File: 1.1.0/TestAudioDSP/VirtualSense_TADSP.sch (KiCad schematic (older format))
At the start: 37 parts, among them P2 CONN_1, P3 CONN_1, P5 CONN_1, P6 CONN_1, P7 uC, P8 uC, U1 MSP430F5435A, U2 24AA1025, U3 PCF2123, U4 24AA025E48, X1 32.6768kHz

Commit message: edited schematics of audio DSP test layer adding libraries of CC5535, DC regulator, AIC3204, 12MHz OSC
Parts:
- removed C1, C10, C11, C2, C3, C4, C7: 100n, symbol CSMALL
- removed C5: 10u, symbol CSMALL
- removed C6: 0,47uF, symbol CSMALL
- removed C8, C9: 18p, symbol CSMALL
- removed FB1, FB2: 10n, symbol FILTER
- removed JP1, JP2, JP3: BREAKER, symbol BREAKER
- removed R1, R2, R9: 47K, symbol R
- removed R7, R8: 10K, symbol R
- removed U1: MSP430F5435A, symbol MSP430F5435A
- removed U2: 24AA1025, symbol 24AA512
- removed U3: PCF2123, symbol PCF2123
- removed U4: 24AA025E48, symbol 24AA512
- removed X1: 32.6768kHz, symbol QUARZO_2PIN
- added U?: TPS77801, symbol TPS77801
- added U?: TPS79501DCQ, symbol TPS79501DCQ
- added U?: DSX321G_12MHZ, symbol DSX321G_12MHZ
- gave numbers to parts that had none: 1
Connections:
- net labels removed: AGND, AVcc, DGND, DVcc, E0_EN/P4.5, E1_EN/P4.4, GNDPWR, RTC_EN/P3.6, RTC_INT/P2.4
- wire segments 245 -> 58
- no-connect marks 17 -> 4
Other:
- moved on the sheet: U2

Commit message: schematics of audio DSP test layer OK, added module on audio DSP test layer brd
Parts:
- removed CONN2, CONN4: CONN_14, symbol CONN_14
- added C1, C16, C17, C23: 4u7, symbol CP1SMALL
- added C10: 33p, symbol CSMALL
- added C11, C12, C20, C21, C7: 10u, symbol CP1SMALL
- added C13, C2: 1u, symbol CSMALL
- added C14, C15, C18, C19, C22, C3, C9: 100n, symbol CSMALL
- added C4, C5: 470n, symbol CSMALL
- added C6, C8: NO, symbol CSMALL
- added JP1: JUMPER, symbol JUMPER
- added L1, L2: BLM21AG151SN1D, symbol FILTER
- added M1: MIC, symbol SPEAKER
- added P1: 1V8CC, symbol CONN_1
- added P4: 1V3CC, symbol CONN_1
- added P9: MC-D, symbol CONN_1
- added Q1: MOS_N, symbol MOS_N
- added R1: 2K2, symbol RSML
- added R10: 110K, symbol RSML
- added R11, R8: 0-NO, symbol RSML
- added R12, R7: 0, symbol RSML
- added R13, R3: 4K7, symbol RSML
- added R14, R15: 300, symbol RSML
- added R2: 1K, symbol RSML
- added R4: 250K, symbol RSML
- added R5: 14K, symbol RSML
- added R6: 30K, symbol RSML
- added R9: 10K7, symbol RSML
- gave numbers to parts that had none: 3
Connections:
- net labels added: CPU_CLK_12MHZ, GND-AIC, GNDPWR, I2C_SCL, I2C_SDA, I2S2_CLK, I2S2_DX, I2S2_FS, I2S2_RX, MCLK, MICN, MICP, TARGET_PWR_GOOD, V3.3A, VCC_1V3, VCC_1V8
- net labels removed: ADC0/P6.0, ADC1/P6.1, ADC2/P6.2, ADC3/P6.3, ADC4/P6.4, ADC5/P6.5, ADC6/P6.6, CLKOUT, DIO2/P8.5, DIO3/P8.6, INT0/P2.0, INT1/P2.3, INT2/P2.5, INT3/P2.6, INT4/P2.7, LED0/P8.0, LED1/P8.1, LED2/P8.2, RXD2/MISO3/P5.7, SCL/P3.2, SDA/P3.1, SN0_EN/P8.3, SN1_EN/P8.4, TXD2/MOSI3/P5.6, VREF+/P5.0, VREF-/P5.1
- wire segments 58 -> 182
- no-connect marks 4 -> 14
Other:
- moved on the sheet: U1, U2, U3, U4

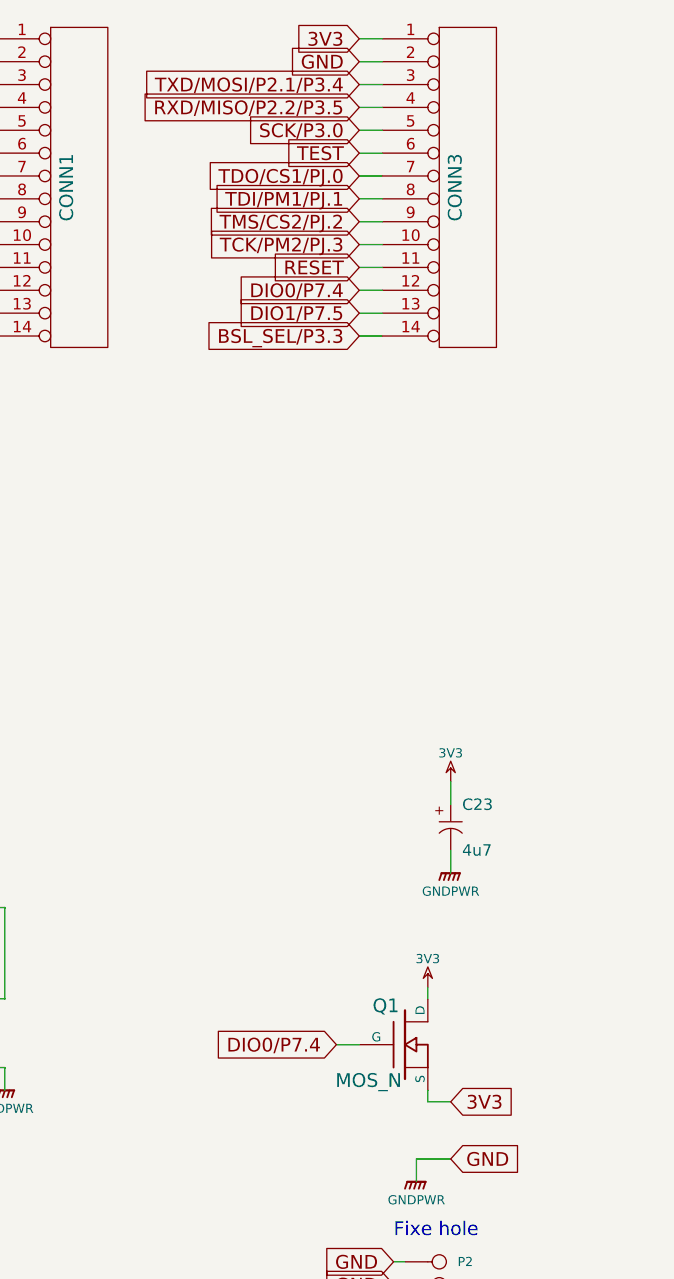
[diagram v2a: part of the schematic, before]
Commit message: audio DSP test layer: brd OK, gerber Ok - sent to PCBoards for check
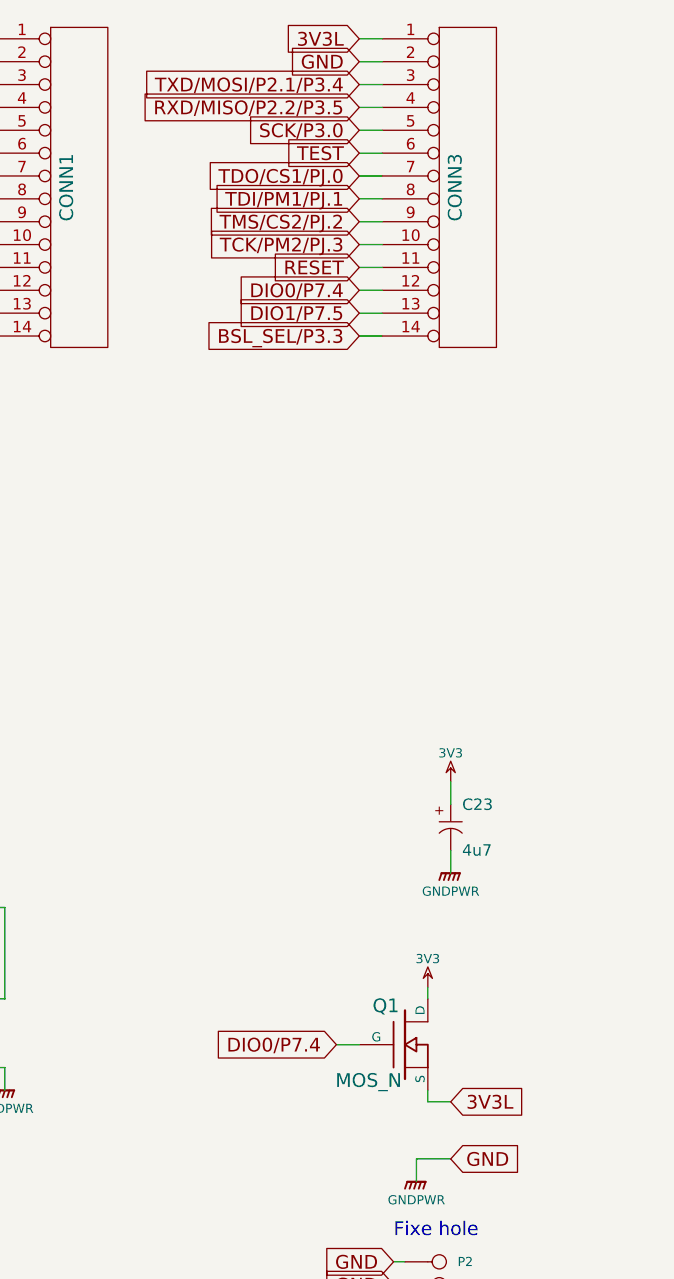
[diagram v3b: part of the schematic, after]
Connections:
- net labels added: 3V3L
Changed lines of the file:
@@
 $EndDescr
 Text GLabel 10400 750  0    60   Input ~ 0
-3V3
+3V3L
 Text GLabel 10400 850  0    60   Input ~ 0
 GND
@@
 $EndSheet
 Text GLabel 10800 5400 2    60   Input ~ 0
-3V3
-$Comp
-L GNDPWR #PWR01
+3V3L
+$Comp
+L GNDPWR #PWR22
 U 1 1 521DAD52
 P 10650 5750
-F 0 "#PWR01" H 10650 5800 40  0001 C CNN
+F 0 "#PWR22" H 10650 5800 40  0001 C CNN
 F 1 "GNDPWR" H 10650 5670 40  0000 C CNN
 F 2 "" H 10650 5750 60  0001 C CNN
@@
 GND
 $Comp
-L GNDPWR #PWR02
+L GNDPWR #PWR4
 U 1 1 521DADD2
 P 1250 1500
-F 0 "#PWR02" H 1250 1550 40  0001 C CNN
+F 0 "#PWR4" H 1250 1550 40  0001 C CNN
 F 1 "GNDPWR" H 1250 1420 40  0000 C CNN
 F 2 "" H 1250 1500 60  0001 C CNN
@@
 $EndComp
 $Comp
-L 3V3 #PWR03
+L 3V3 #PWR1
 U 1 1 521DAE7E
 P 1000 1050
-F 0 "#PWR03" H 1000 1150 40  0001 C CNN
+F 0 "#PWR1" H 1000 1150 40  0001 C CNN
 F 1 "3V3" H 1000 1175 40  0000 C CNN
 F 2 "" H 1000 1050 60  0001 C CNN
@@
 $EndComp
 $Comp
-L GNDPWR #PWR04
+L GNDPWR #PWR10
 U 1 1 521DB683
 P 3350 1900
-F 0 "#PWR04" H 3350 1950 40  0001 C CNN
+F 0 "#PWR10" H 3350 1950 40  0001 C CNN
 F 1 "GNDPWR" H 3350 1820 40  0000 C CNN
 F 2 "" H 3350 1900 60  0001 C CNN
@@
 $EndComp
 $Comp
-L GNDPWR #PWR05
+L GNDPWR #PWR14
 U 1 1 521DB7CE
 P 3650 1600
-F 0 "#PWR05" H 3650 1650 40  0001 C CNN
+F 0 "#PWR14" H 3650 1650 40  0001 C CNN
 F 1 "GNDPWR" H 3650 1520 40  0000 C CNN
 F 2 "" H 3650 1600 60  0001 C CNN
@@
 VCC_1V3
 $Comp
-L 3V3 #PWR06
+L 3V3 #PWR8
 U 1 1 521DB933
 P 2950 1500
-F 0 "#PWR06" H 2950 1600 40  0001 C CNN
+F 0 "#PWR8" H 2950 1600 40  0001 C CNN
 F 1 "3V3" H 2950 1625 40  0000 C CNN
 F 2 "" H 2950 1500 60  0001 C CNN
@@
 TARGET_PWR_GOOD
 $Comp
-L 3V3 #PWR07
+L 3V3 #PWR2
 U 1 1 521DBAC4
 P 1000 2300
-F 0 "#PWR07" H 1000 2400 40  0001 C CNN
+F 0 "#PWR2" H 1000 2400 40  0001 C CNN
 F 1 "3V3" H 1000 2425 40  0000 C CNN
 F 2 "" H 1000 2300 60  0001 C CNN
@@
 $EndComp
 $Comp
-L GNDPWR #PWR08
+L GNDPWR #PWR3
 U 1 1 521DBAF7
 P 1000 2750
-F 0 "#PWR08" H 1000 2800 40  0001 C CNN
+F 0 "#PWR3" H 1000 2800 40  0001 C CNN
 F 1 "GNDPWR" H 1000 2670 40  0000 C CNN
 F 2 "" H 1000 2750 60  0001 C CNN
@@
 $EndComp
 $Comp
-L GNDPWR #PWR09
+L GNDPWR #PWR6
 U 1 1 521DBFAD
 P 2200 3050
-F 0 "#PWR09" H 2200 3100 40  0001 C CNN
+F 0 "#PWR6" H 2200 3100 40  0001 C CNN
 F 1 "GNDPWR" H 2200 2970 40  0000 C CNN
 F 2 "" H 2200 3050 60  0001 C CNN
@@
 $EndComp
 $Comp
-L GNDPWR #PWR010
+L GNDPWR #PWR12
 U 1 1 521DC2F6
 P 3550 2750
-F 0 "#PWR010" H 3550 2800 40  0001 C CNN
+F 0 "#PWR12" H 3550 2800 40  0001 C CNN
 F 1 "GNDPWR" H 3550 2670 40  0000 C CNN
 F 2 "" H 3550 2750 60  0001 C CNN
@@
 VCC_1V8
 $Comp
-L GNDPWR #PWR011
+L GNDPWR #PWR9
 U 1 1 521DC78D
 P 3000 3150
-F 0 "#PWR011" H 3000 3200 40  0001 C CNN
+F 0 "#PWR9" H 3000 3200 40  0001 C CNN
 F 1 "GNDPWR" H 3000 3070 40  0000 C CNN
 F 2 "" H 3000 3150 60  0001 C CNN
@@
 $EndComp
 $Comp
-L 3V3 #PWR012
+L 3V3 #PWR24
 U 1 1 521DCB4A
 P 10800 4000
-F 0 "#PWR012" H 10800 4100 40  0001 C CNN
+F 0 "#PWR24" H 10800 4100 40  0001 C CNN
 F 1 "3V3" H 10800 4125 40  0000 C CNN
 F 2 "" H 10800 4000 60  0001 C CNN
@@
 $EndComp
 $Comp
-L GNDPWR #PWR013
+L GNDPWR #PWR25
 U 1 1 521DCB50
 P 10800 4400
-F 0 "#PWR013" H 10800 4450 40  0001 C CNN
+F 0 "#PWR25" H 10800 4450 40  0001 C CNN
 F 1 "GNDPWR" H 10800 4320 40  0000 C CNN
 F 2 "" H 10800 4400 60  0001 C CNN
@@
 $EndComp
 $Comp
-L GNDPWR #PWR014
+L GNDPWR #PWR11
 U 1 1 521DCE8E
 P 3350 4450
-F 0 "#PWR014" H 3350 4500 40  0001 C CNN
+F 0 "#PWR11" H 3350 4500 40  0001 C CNN
 F 1 "GNDPWR" H 3350 4370 40  0000 C CNN
 F 2 "" H 3350 4450 60  0001 C CNN
@@
 $EndComp
 $Comp
-L 3V3 #PWR015
+L 3V3 #PWR7
 U 1 1 521DCFCF
 P 2800 4100
-F 0 "#PWR015" H 2800 4200 40  0001 C CNN
+F 0 "#PWR7" H 2800 4200 40  0001 C CNN
 F 1 "3V3" H 2800 4225 40  0000 C CNN
 F 2 "" H 2800 4100 60  0001 C CNN
@@
 $EndComp
 $Comp
-L GNDPWR #PWR016
+L GNDPWR #PWR19
 U 1 1 521DD2BC
 P 7150 6900
-F 0 "#PWR016" H 7150 6950 40  0001 C CNN
+F 0 "#PWR19" H 7150 6950 40  0001 C CNN
 F 1 "GNDPWR" H 7150 6820 40  0000 C CNN
 F 2 "" H 7150 6900 60  0001 C CNN
@@
 $EndComp
 $Comp
-L 3V3 #PWR017
+L 3V3 #PWR21
 U 1 1 521DD2C2
 P 8850 6800
-F 0 "#PWR017" H 8850 6900 40  0001 C CNN
+F 0 "#PWR21" H 8850 6900 40  0001 C CNN
 F 1 "3V3" H 8850 6925 40  0000 C CNN
 F 2 "" H 8850 6800 60  0001 C CNN
@@
 $EndComp
 $Comp
-L GNDPWR #PWR018
+L GNDPWR #PWR13
 U 1 1 521DDF50
 P 3600 3950
-F 0 "#PWR018" H 3600 4000 40  0001 C CNN
+F 0 "#PWR13" H 3600 4000 40  0001 C CNN
 F 1 "GNDPWR" H 3600 3870 40  0000 C CNN
 F 2 "" H 3600 3950 60  0001 C CNN
@@
 $EndComp
 $Comp
-L GNDPWR #PWR019
+L GNDPWR #PWR15
 U 1 1 521DE36F
 P 3850 7000
-F 0 "#PWR019" H 3850 7050 40  0001 C CNN
+F 0 "#PWR15" H 3850 7050 40  0001 C CNN
 F 1 "GNDPWR" H 3850 6920 40  0000 C CNN
 F 2 "" H 3850 7000 60  0001 C CNN
@@
 NoConn ~ 3250 6300
 $Comp
-L 3V3 #PWR020
+L 3V3 #PWR5
 U 1 1 521DECC8
 P 2100 6150
-F 0 "#PWR020" H 2100 6250 40  0001 C CNN
+F 0 "#PWR5" H 2100 6250 40  0001 C CNN
 F 1 "3V3" H 2100 6275 40  0000 C CNN
 F 2 "" H 2100 6150 60  0001 C CNN
@@
 $EndComp
 $Comp
-L GNDPWR #PWR021
+L GNDPWR #PWR16
 U 1 1 521DFB68
 P 5300 6550
-F 0 "#PWR021" H 5300 6600 40  0001 C CNN
+F 0 "#PWR16" H 5300 6600 40  0001 C CNN
 F 1 "GNDPWR" H 5300 6470 40  0000 C CNN
 F 2 "" H 5300 6550 60  0001 C CNN
@@
 I2S2_CLK
 $Comp
-L 3V3 #PWR022
+L 3V3 #PWR17
 U 1 1 521E0515
 P 6900 4500
-F 0 "#PWR022" H 6900 4600 40  0001 C CNN
+F 0 "#PWR17" H 6900 4600 40  0001 C CNN
 F 1 "3V3" H 6900 4625 40  0000 C CNN
 F 2 "" H 6900 4500 60  0001 C CNN
@@
 $EndComp
 $Comp
-L GNDPWR #PWR023
+L GNDPWR #PWR18
 U 1 1 521E0521
 P 6900 4900
-F 0 "#PWR023" H 6900 4950 40  0001 C CNN
+F 0 "#PWR18" H 6900 4950 40  0001 C CNN
 F 1 "GNDPWR" H 6900 4820 40  0000 C CNN
 F 2 "" H 6900 4900 60  0001 C CNN
@@
 $EndComp
 $Comp
-L GNDPWR #PWR024
+L GNDPWR #PWR20
 U 1 1 521E091E
 P 8850 5350
-F 0 "#PWR024" H 8850 5400 40  0001 C CNN
+F 0 "#PWR20" H 8850 5400 40  0001 C CNN
 F 1 "GNDPWR" H 8850 5270 40  0000 C CNN
 F 2 "" H 8850 5350 60  0001 C CNN
@@
 $EndComp
 $Comp
-L 3V3 #PWR025
+L 3V3 #PWR23
 U 1 1 521E0E79
 P 10700 4900
-F 0 "#PWR025" H 10700 5000 40  0001 C CNN
+F 0 "#PWR23" H 10700 5000 40  0001 C CNN
 F 1 "3V3" H 10700 5025 40  0000 C CNN
 F 2 "" H 10700 4900 60  0001 C CNN

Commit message: audio DSP test layer: renamed zip first gerber, added 0-Ohm (R35) for module U2, schematic OK, brd OK, gerber OK - 2nd sent to PCBoards for check
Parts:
- removed P9: MC-D, symbol CONN_1
- added R35: 0, symbol RSML
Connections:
- wire segments 182 -> 184
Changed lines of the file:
@@
 3V3L
 $Comp
-L GNDPWR #PWR22
+L GNDPWR #PWR01
 U 1 1 521DAD52
 P 10650 5750
-F 0 "#PWR22" H 10650 5800 40  0001 C CNN
+F 0 "#PWR01" H 10650 5800 40  0001 C CNN
 F 1 "GNDPWR" H 10650 5670 40  0000 C CNN
 F 2 "" H 10650 5750 60  0001 C CNN
@@
 GND
 $Comp
-L GNDPWR #PWR4
+L GNDPWR #PWR02
 U 1 1 521DADD2
 P 1250 1500
-F 0 "#PWR4" H 1250 1550 40  0001 C CNN
+F 0 "#PWR02" H 1250 1550 40  0001 C CNN
 F 1 "GNDPWR" H 1250 1420 40  0000 C CNN
 F 2 "" H 1250 1500 60  0001 C CNN
@@
 $EndComp
 $Comp
-L 3V3 #PWR1
+L 3V3 #PWR03
 U 1 1 521DAE7E
 P 1000 1050
-F 0 "#PWR1" H 1000 1150 40  0001 C CNN
+F 0 "#PWR03" H 1000 1150 40  0001 C CNN
 F 1 "3V3" H 1000 1175 40  0000 C CNN
 F 2 "" H 1000 1050 60  0001 C CNN
@@
 $EndComp
 $Comp
-L GNDPWR #PWR10
+L GNDPWR #PWR04
 U 1 1 521DB683
 P 3350 1900
-F 0 "#PWR10" H 3350 1950 40  0001 C CNN
+F 0 "#PWR04" H 3350 1950 40  0001 C CNN
 F 1 "GNDPWR" H 3350 1820 40  0000 C CNN
 F 2 "" H 3350 1900 60  0001 C CNN
@@
 $EndComp
 $Comp
-L GNDPWR #PWR14
+L GNDPWR #PWR05
 U 1 1 521DB7CE
 P 3650 1600
-F 0 "#PWR14" H 3650 1650 40  0001 C CNN
+F 0 "#PWR05" H 3650 1650 40  0001 C CNN
 F 1 "GNDPWR" H 3650 1520 40  0000 C CNN
 F 2 "" H 3650 1600 60  0001 C CNN
@@
 VCC_1V3
 $Comp
-L 3V3 #PWR8
+L 3V3 #PWR06
 U 1 1 521DB933
 P 2950 1500
-F 0 "#PWR8" H 2950 1600 40  0001 C CNN
+F 0 "#PWR06" H 2950 1600 40  0001 C CNN
 F 1 "3V3" H 2950 1625 40  0000 C CNN
 F 2 "" H 2950 1500 60  0001 C CNN
@@
 TARGET_PWR_GOOD
 $Comp
-L 3V3 #PWR2
+L 3V3 #PWR07
 U 1 1 521DBAC4
 P 1000 2300
-F 0 "#PWR2" H 1000 2400 40  0001 C CNN
+F 0 "#PWR07" H 1000 2400 40  0001 C CNN
 F 1 "3V3" H 1000 2425 40  0000 C CNN
 F 2 "" H 1000 2300 60  0001 C CNN
@@
 $EndComp
 $Comp
-L GNDPWR #PWR3
+L GNDPWR #PWR08
 U 1 1 521DBAF7
 P 1000 2750
-F 0 "#PWR3" H 1000 2800 40  0001 C CNN
+F 0 "#PWR08" H 1000 2800 40  0001 C CNN
 F 1 "GNDPWR" H 1000 2670 40  0000 C CNN
 F 2 "" H 1000 2750 60  0001 C CNN
@@
 $EndComp
 $Comp
-L GNDPWR #PWR6
+L GNDPWR #PWR09
 U 1 1 521DBFAD
 P 2200 3050
-F 0 "#PWR6" H 2200 3100 40  0001 C CNN
+F 0 "#PWR09" H 2200 3100 40  0001 C CNN
 F 1 "GNDPWR" H 2200 2970 40  0000 C CNN
 F 2 "" H 2200 3050 60  0001 C CNN
@@
 $EndComp
 $Comp
-L GNDPWR #PWR12
+L GNDPWR #PWR010
 U 1 1 521DC2F6
 P 3550 2750
-F 0 "#PWR12" H 3550 2800 40  0001 C CNN
+F 0 "#PWR010" H 3550 2800 40  0001 C CNN
 F 1 "GNDPWR" H 3550 2670 40  0000 C CNN
 F 2 "" H 3550 2750 60  0001 C CNN
@@
 VCC_1V8
 $Comp
-L GNDPWR #PWR9
+L GNDPWR #PWR011
 U 1 1 521DC78D
 P 3000 3150
-F 0 "#PWR9" H 3000 3200 40  0001 C CNN
+F 0 "#PWR011" H 3000 3200 40  0001 C CNN
 F 1 "GNDPWR" H 3000 3070 40  0000 C CNN
 F 2 "" H 3000 3150 60  0001 C CNN
@@
 $EndComp
 $Comp
-L 3V3 #PWR24
+L 3V3 #PWR012
 U 1 1 521DCB4A
 P 10800 4000
-F 0 "#PWR24" H 10800 4100 40  0001 C CNN
+F 0 "#PWR012" H 10800 4100 40  0001 C CNN
 F 1 "3V3" H 10800 4125 40  0000 C CNN
 F 2 "" H 10800 4000 60  0001 C CNN
@@
 $EndComp
 $Comp
-L GNDPWR #PWR25
+L GNDPWR #PWR013
 U 1 1 521DCB50
 P 10800 4400
-F 0 "#PWR25" H 10800 4450 40  0001 C CNN
+F 0 "#PWR013" H 10800 4450 40  0001 C CNN
 F 1 "GNDPWR" H 10800 4320 40  0000 C CNN
 F 2 "" H 10800 4400 60  0001 C CNN
@@
 $EndComp
 $Comp
-L GNDPWR #PWR11
+L GNDPWR #PWR014
 U 1 1 521DCE8E
 P 3350 4450
-F 0 "#PWR11" H 3350 4500 40  0001 C CNN
+F 0 "#PWR014" H 3350 4500 40  0001 C CNN
 F 1 "GNDPWR" H 3350 4370 40  0000 C CNN
 F 2 "" H 3350 4450 60  0001 C CNN
@@
 $EndComp
 $Comp
-L 3V3 #PWR7
+L 3V3 #PWR015
 U 1 1 521DCFCF
 P 2800 4100
-F 0 "#PWR7" H 2800 4200 40  0001 C CNN
+F 0 "#PWR015" H 2800 4200 40  0001 C CNN
 F 1 "3V3" H 2800 4225 40  0000 C CNN
 F 2 "" H 2800 4100 60  0001 C CNN
@@
 $EndComp
 $Comp
-L GNDPWR #PWR19
+L GNDPWR #PWR016
 U 1 1 521DD2BC
 P 7150 6900
-F 0 "#PWR19" H 7150 6950 40  0001 C CNN
+F 0 "#PWR016" H 7150 6950 40  0001 C CNN
 F 1 "GNDPWR" H 7150 6820 40  0000 C CNN
 F 2 "" H 7150 6900 60  0001 C CNN
@@
 $EndComp
 $Comp
-L 3V3 #PWR21
+L 3V3 #PWR017
 U 1 1 521DD2C2
 P 8850 6800
-F 0 "#PWR21" H 8850 6900 40  0001 C CNN
+F 0 "#PWR017" H 8850 6900 40  0001 C CNN
 F 1 "3V3" H 8850 6925 40  0000 C CNN
 F 2 "" H 8850 6800 60  0001 C CNN
@@
 $EndComp
 $Comp
-L GNDPWR #PWR13
+L GNDPWR #PWR018
 U 1 1 521DDF50
 P 3600 3950
-F 0 "#PWR13" H 3600 4000 40  0001 C CNN
+F 0 "#PWR018" H 3600 4000 40  0001 C CNN
 F 1 "GNDPWR" H 3600 3870 40  0000 C CNN
 F 2 "" H 3600 3950 60  0001 C CNN
@@
 $EndComp
 $Comp
-L GNDPWR #PWR15
+L GNDPWR #PWR019
 U 1 1 521DE36F
 P 3850 7000
-F 0 "#PWR15" H 3850 7050 40  0001 C CNN
+F 0 "#PWR019" H 3850 7050 40  0001 C CNN
 F 1 "GNDPWR" H 3850 6920 40  0000 C CNN
 F 2 "" H 3850 7000 60  0001 C CNN
@@
 NoConn ~ 3250 6300
 $Comp
-L 3V3 #PWR5
+L 3V3 #PWR020
 U 1 1 521DECC8
 P 2100 6150
-F 0 "#PWR5" H 2100 6250 40  0001 C CNN
+F 0 "#PWR020" H 2100 6250 40  0001 C CNN
 F 1 "3V3" H 2100 6275 40  0000 C CNN
 F 2 "" H 2100 6150 60  0001 C CNN
@@
 $EndComp
 $Comp
-L GNDPWR #PWR16
+L GNDPWR #PWR021
 U 1 1 521DFB68
 P 5300 6550
-F 0 "#PWR16" H 5300 6600 40  0001 C CNN
+F 0 "#PWR021" H 5300 6600 40  0001 C CNN
 F 1 "GNDPWR" H 5300 6470 40  0000 C CNN
 F 2 "" H 5300 6550 60  0001 C CNN
@@
 I2S2_CLK
 $Comp
-L 3V3 #PWR17
+L 3V3 #PWR022
 U 1 1 521E0515
 P 6900 4500
-F 0 "#PWR17" H 6900 4600 40  0001 C CNN
+F 0 "#PWR022" H 6900 4600 40  0001 C CNN
 F 1 "3V3" H 6900 4625 40  0000 C CNN
 F 2 "" H 6900 4500 60  0001 C CNN
@@
 $EndComp
 $Comp
-L GNDPWR #PWR18
+L GNDPWR #PWR023
 U 1 1 521E0521
 P 6900 4900
-F 0 "#PWR18" H 6900 4950 40  0001 C CNN
+F 0 "#PWR023" H 6900 4950 40  0001 C CNN
 F 1 "GNDPWR" H 6900 4820 40  0000 C CNN
 F 2 "" H 6900 4900 60  0001 C CNN
@@
 $EndComp
 $Comp
-L GNDPWR #PWR20
+L GNDPWR #PWR024
 U 1 1 521E091E
 P 8850 5350
-F 0 "#PWR20" H 8850 5400 40  0001 C CNN
+F 0 "#PWR024" H 8850 5400 40  0001 C CNN
 F 1 "GNDPWR" H 8850 5270 40  0000 C CNN
 F 2 "" H 8850 5350 60  0001 C CNN
@@
 $EndComp
 $Comp
-L 3V3 #PWR23
+L 3V3 #PWR025
 U 1 1 521E0E79
 P 10700 4900
-F 0 "#PWR23" H 10700 5000 40  0001 C CNN
+F 0 "#PWR025" H 10700 5000 40  0001 C CNN
 F 1 "3V3" H 10700 5025 40  0000 C CNN
 F 2 "" H 10700 4900 60  0001 C CNN
@@
 	0    -1   -1   0
 $EndComp
-$Comp
-L CONN_1 P9
-U 1 1 521F5C88
-P 4900 6450
-F 0 "P9" H 4980 6450 40  0000 L CNN
-F 1 "MC-D" H 4900 6505 30  0001 C CNN
-F 2 "" H 4900 6450 60  0000 C CNN
-F 3 "" H 4900 6450 60  0000 C CNN
-	1    4900 6450
-	0    1    1    0
-$EndComp
 Wire Wire Line
 	10550 6100 10600 6100
@@
 Wire Wire Line
 	4850 6300 4900 6300
+$Comp
+L RSML R35
+U 1 1 522EF121
+P 4900 6500
+F 0 "R35" V 4980 6500 40  0000 C CNN
+F 1 "0" V 4902 6500 40  0000 C CNN
+F 2 "" V 4830 6500 30  0000 C CNN
+F 3 "" H 4900 6500 30  0000 C CNN
+	1    4900 6500
+	-1   0    0    1
+$EndComp
+$Comp
+L GNDPWR #PWR026
+U 1 1 522EF136
+P 4900 6750
+F 0 "#PWR026" H 4900 6800 40  0001 C CNN
+F 1 "GNDPWR" H 4900 6670 40  0000 C CNN
+F 2 "" H 4900 6750 60  0001 C CNN
+F 3 "" H 4900 6750 60  0001 C CNN
+	1    4900 6750
+	1    0    0    -1
+$EndComp
+Wire Wire Line
+	4900 6300 4900 6350
+Wire Wire Line
+	4900 6650 4900 6750
 $EndSCHEMATC
